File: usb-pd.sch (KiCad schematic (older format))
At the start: 32 parts, among them J12 12401598E4_2A, Q7 SQS401EN-T1_BE3, U18 STUSB4500QTR

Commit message: Loclib
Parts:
- J12: footprint antmicro-footprints:USB-C_Female_12401X -> sa800u-baseboard-hw-footprints:USB-C_Female_12401X; symbol antmicroUSBDVIHDMIConnectors:12401598E4_2A -> sa800u-baseboard-hw:12401598E4_2A
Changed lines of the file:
@@
 NoConn ~ 4650 4600
 $Comp
-L antmicroUSBDVIHDMIConnectors:12401598E4_2A J12
+L sa800u-baseboard-hw:12401598E4_2A J12
 U 1 1 6220D088
 P 3150 2500
 F 0 "J12" H 3150 3535 50  0000 C CNN
 F 1 "12401598E4_2A" H 3150 3444 50  0000 C CNN
-F 2 "antmicro-footprints:USB-C_Female_12401X" H 3350 2700 60  0001 L CNN
+F 2 "sa800u-baseboard-hw-footprints:USB-C_Female_12401X" H 3350 2700 60  0001 L CNN
 F 3 "http://www.amphenol-icc.com/media/wysiwyg/files/drawing/12401598xxx2a.pdf" H 3350 2800 60  0001 L CNN
 F 4 "12401598E4#2A" H 3350 3000 60  0001 L CNN "MPN"

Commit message: Change diode to larger footprint
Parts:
- removed D28: ESD144B1W0201E6327XTSA1, sa800u-baseboard-hw-footprints:ESD144B1W0201E6327XTSA1, symbol sa800u-baseboard-hw:ESD144B1W0201E6327XTSA1
- added D1: PESD18VF1BSFYL, antmicro-footprints:RESC0603X26N, symbol antmicroTVSDiodes:PESD18VF1BSFYL
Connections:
- wire segments 135 -> 136
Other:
- moved on the sheet: R106
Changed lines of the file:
@@
 L sa800u-baseboard-hw:R_470R_0402 R106
 U 1 1 61E425A4
-P 7225 1325
-F 0 "R106" V 7180 1256 60  0000 R CNN
-F 1 "R_470R_0402" H 7225 1175 60  0001 C CNN
-F 2 "sa800u-baseboard-hw-footprints:0402-res" H 7425 1525 60  0001 L CNN
-F 3 "" H 7225 1325 50  0001 C CNN
-F 4 "VISHAY" H 7425 1725 60  0001 L CNN "Manufacturer"
-F 5 "CRCW0402470RFKED" H 7425 1625 60  0001 L CNN "MPN"
-F 6 "470R" V 7278 1256 50  0000 R CNN "Val"
-	1    7225 1325
+P 7150 2050
+F 0 "R106" V 7105 1981 60  0000 R CNN
+F 1 "R_470R_0402" H 7150 1900 60  0001 C CNN
+F 2 "sa800u-baseboard-hw-footprints:0402-res" H 7350 2250 60  0001 L CNN
+F 3 "" H 7150 2050 50  0001 C CNN
+F 4 "VISHAY" H 7350 2450 60  0001 L CNN "Manufacturer"
+F 5 "CRCW0402470RFKED" H 7350 2350 60  0001 L CNN "MPN"
+F 6 "470R" V 7203 1981 50  0000 R CNN "Val"
+	1    7150 2050
 	0    1    1    0
 $EndComp
@@
 NoConn ~ 3650 2050
 NoConn ~ 3650 2150
-$Comp
-L sa800u-baseboard-hw:ESD144B1W0201E6327XTSA1 D28
-U 1 1 630E4F56
-P 11350 2100
-F 0 "D28" V 11304 2178 50  0000 L CNN
-F 1 "ESD144B1W0201E6327XTSA1" V 11395 2178 50  0000 L CNN
-F 2 "sa800u-baseboard-hw-footprints:ESD144B1W0201E6327XTSA1" H 11350 2100 50  0001 C CNN
-F 3 "https://www.infineon.com/dgdl/Infineon-ESD144-B1-W0201-DataSheet-v02_00-EN.pdf?fileId=5546d462677d0f4601679886a2a8707c" H 11350 2100 50  0001 C CNN
-F 4 "ESD144B1W0201E6327XTSA1" H 11350 2100 50  0001 C CNN "MPN"
-F 5 "Infineon Technologies" H 11350 2100 50  0001 C CNN "Manufacturer"
-	1    11350 2100
-	0    1    1    0
-$EndComp
-Wire Wire Line
-	10950 1750 11350 1750
-Wire Wire Line
-	11350 1750 11800 1750
-Connection ~ 11350 1750
 Wire Wire Line
 	11350 2450 11350 2500
@@
 Wire Wire Line
 	8700 2450 9400 2450
+$Comp
+L antmicroTVSDiodes:PESD18VF1BSFYL D1
+U 1 1 622DA21E
+P 11350 2200
+F 0 "D1" V 11309 2303 60  0000 L CNN
+F 1 "PESD18VF1BSFYL" V 11415 2303 60  0000 L CNN
+F 2 "antmicro-footprints:RESC0603X26N" H 11350 1750 100 0001 L CNN
+F 3 "https://www.mouser.pl/datasheet/2/916/PESD18VF1BSF-1599696.pdf" H 11560 2050 100 0001 C CNN
+F 4 "nexperia" H 11350 1625 100 0001 L CNN "Manufacturer"
+F 5 "PESD18VF1BSFYL" H 11350 1875 100 0001 L CNN "MPN"
+	1    11350 2200
+	0    1    1    0
+$EndComp
+Wire Wire Line
+	10950 1750 11350 1750
+Wire Wire Line
+	11350 1975 11350 1750
+Connection ~ 11350 1750
+Wire Wire Line
+	11350 1750 11800 1750
 $EndSCHEMATC

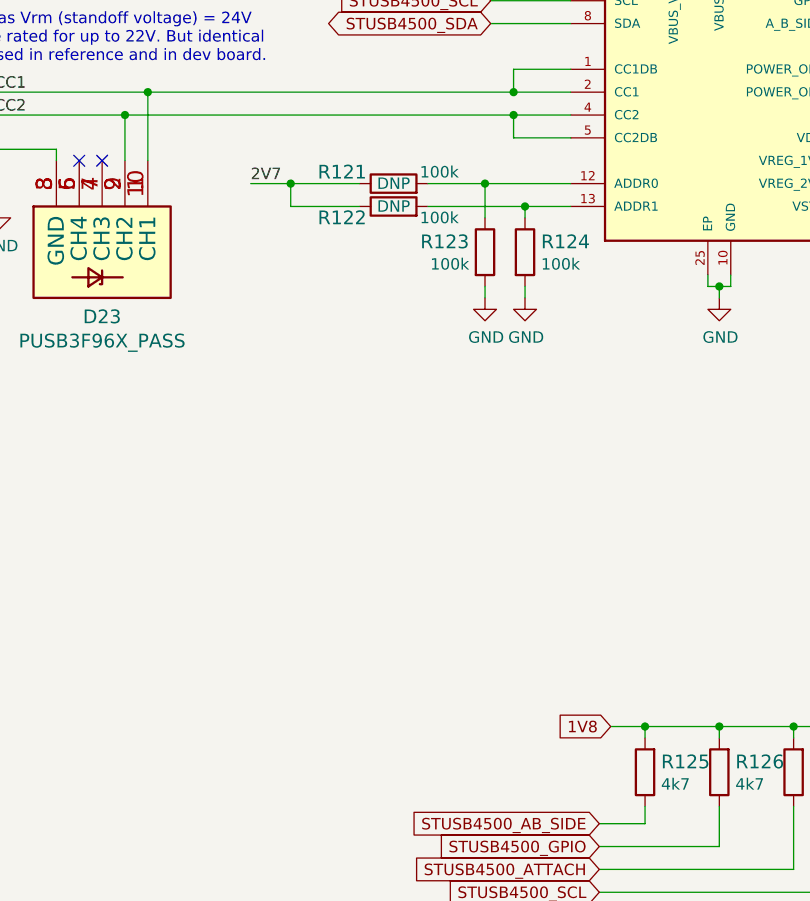
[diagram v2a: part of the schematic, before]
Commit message: Fix 2V7 label naming
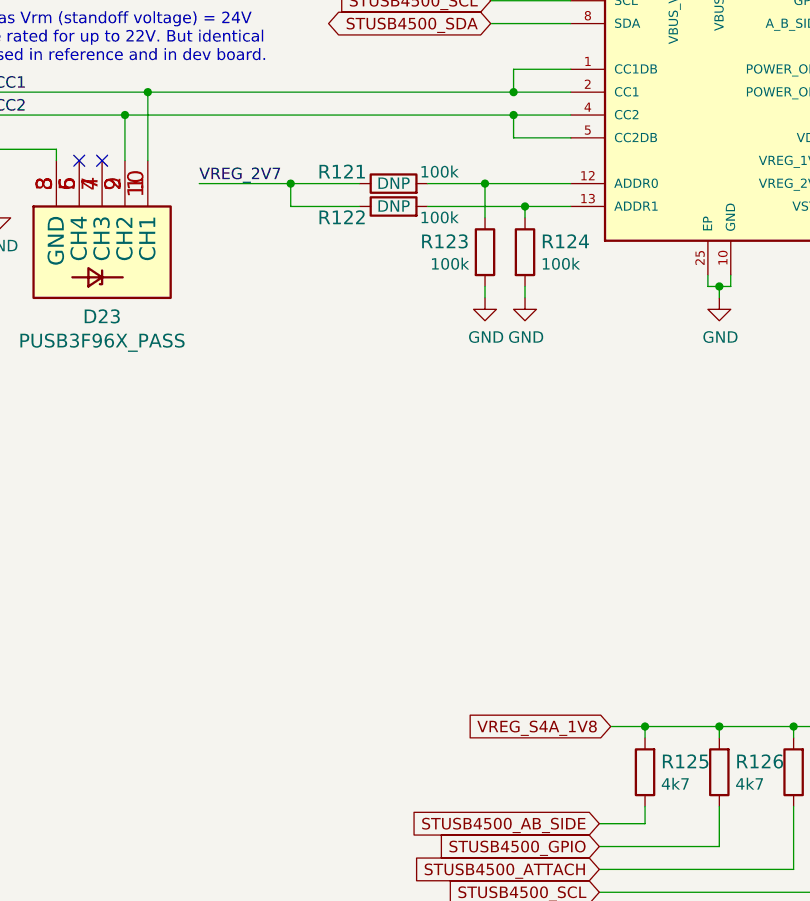
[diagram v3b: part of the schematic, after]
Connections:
- net labels added: VREG_S4A_1V8
- net labels removed: 1V8, 2V7
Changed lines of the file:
@@
 Wire Wire Line
 	5475 4800 5775 4800
-Text Label 5300 4700 0    50   ~ 0
-2V7
 $Comp
 L sa800u-baseboard-hw:R_100k_0402 R121
@@
 Text GLabel 6825 7500 0    50   Input ~ 0
 STUSB4500_AB_SIDE
-Text GLabel 6875 7075 0    50   Input ~ 0
-1V8
 Wire Wire Line
 	7025 7075 6875 7075
@@
 Connection ~ 7350 5150
 Wire Wire Line
-	5300 4700 5475 4700
+	5075 4700 5475 4700
 Connection ~ 5475 4700
 Wire Wire Line
@@
 Wire Wire Line
 	11350 1750 11800 1750
+Text GLabel 6875 7075 0    50   Input ~ 0
+VREG_S4A_1V8
+Text Label 5075 4700 0    50   ~ 0
+VREG_2V7
 $EndSCHEMATC

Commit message: Loclib
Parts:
- D1: footprint antmicro-footprints:RESC0603X26N -> sa800u-baseboard-hw-footprints:RESC0603X26N; symbol antmicroTVSDiodes:PESD18VF1BSFYL -> sa800u-baseboard-hw:PESD18VF1BSFYL
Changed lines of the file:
@@
 	8700 2450 9400 2450
 $Comp
-L antmicroTVSDiodes:PESD18VF1BSFYL D1
+L sa800u-baseboard-hw:PESD18VF1BSFYL D1
 U 1 1 622DA21E
 P 11350 2200
 F 0 "D1" V 11309 2303 60  0000 L CNN
 F 1 "PESD18VF1BSFYL" V 11415 2303 60  0000 L CNN
-F 2 "antmicro-footprints:RESC0603X26N" H 11350 1750 100 0001 L CNN
+F 2 "sa800u-baseboard-hw-footprints:RESC0603X26N" H 11350 1750 100 0001 L CNN
 F 3 "https://www.mouser.pl/datasheet/2/916/PESD18VF1BSF-1599696.pdf" H 11560 2050 100 0001 C CNN
 F 4 "nexperia" H 11350 1625 100 0001 L CNN "Manufacturer"
